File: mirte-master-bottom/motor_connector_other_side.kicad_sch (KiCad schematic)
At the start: 9 parts, among them J8 Motor_conn, U4 DRV8231DDAR

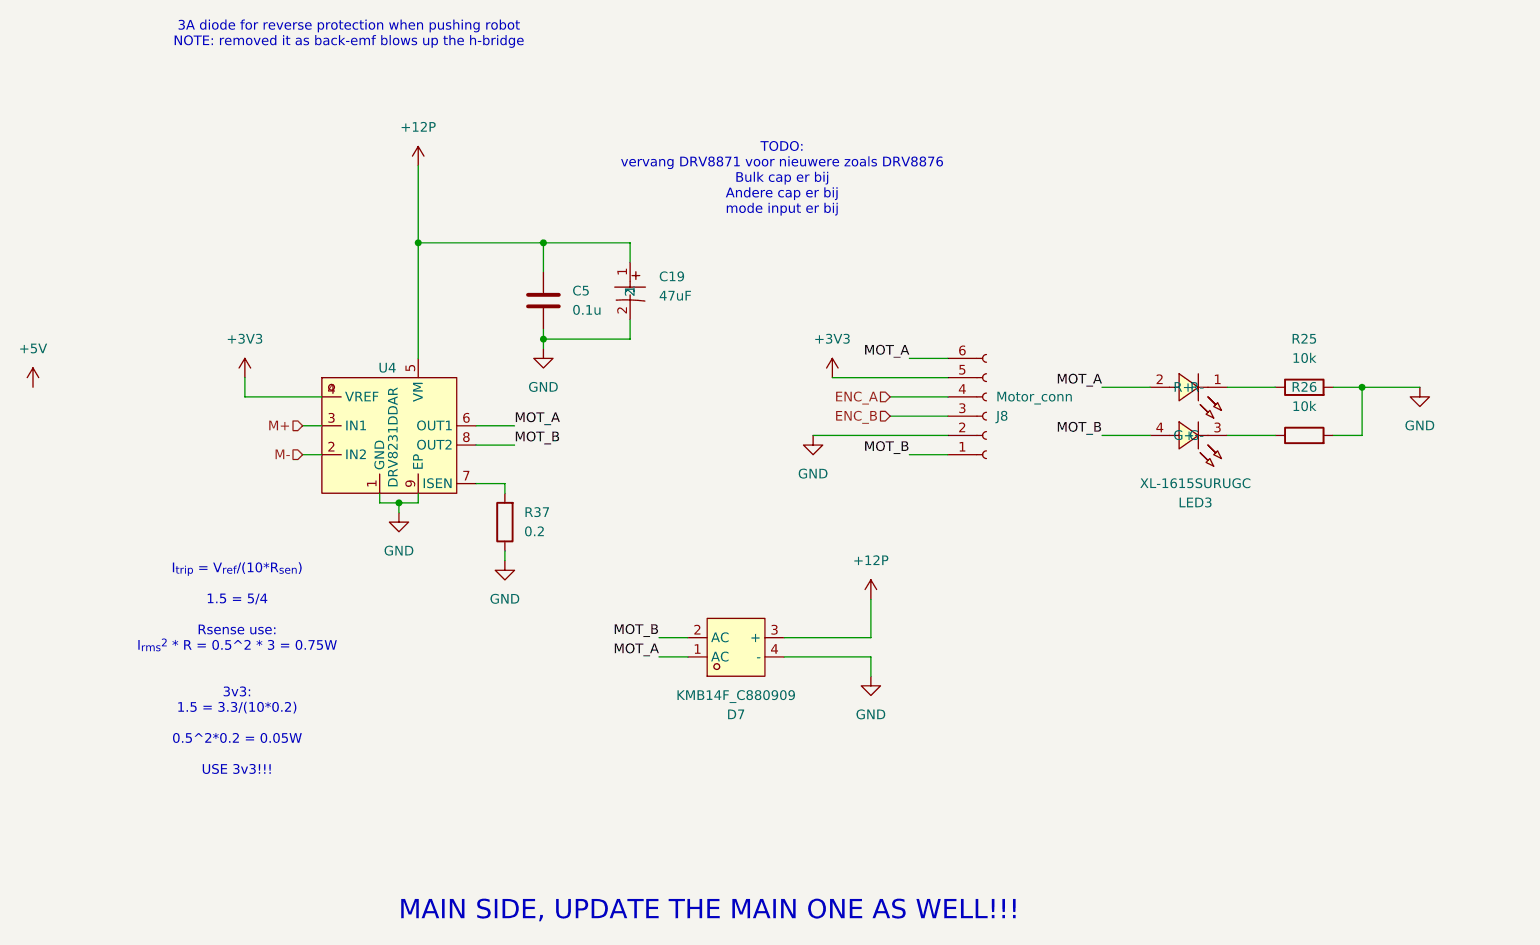
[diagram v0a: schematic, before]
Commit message: MM: motor leds same color, emergency button screw, start button led screw, drc exclusions
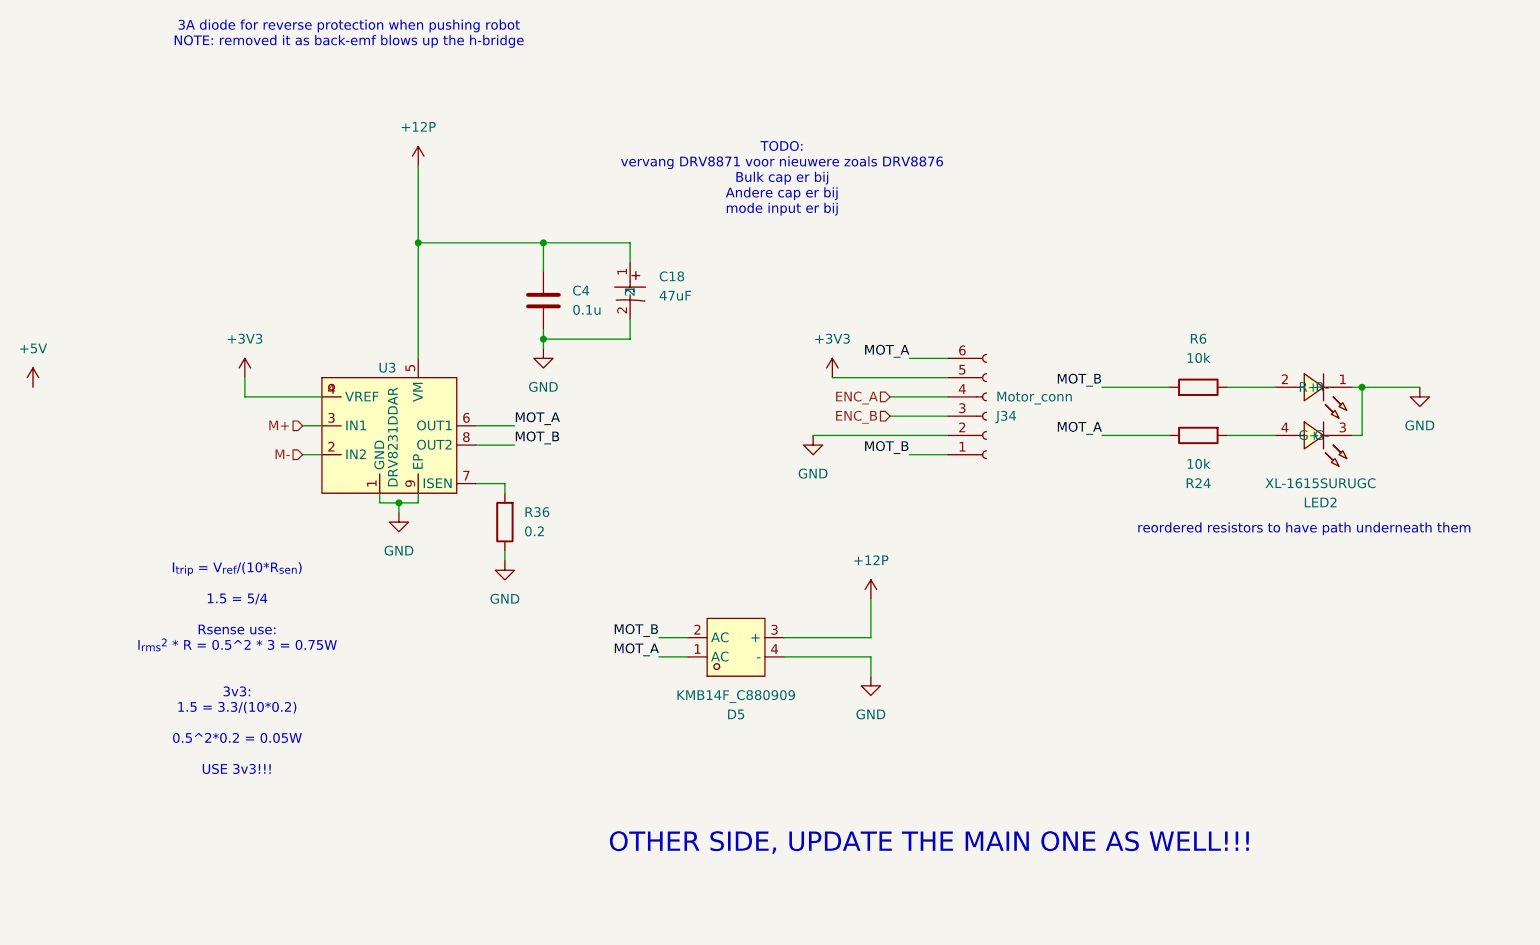
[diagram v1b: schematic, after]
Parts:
- renumbered C19 to C18, C5 to C4, D7 to D5, J8 to J34, LED3 to LED2, R26 to R24, R37 to R36, R25 to R6, U4 to U3
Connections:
- net GND: now also LED2.1 (R-), LED2.3 (G-); no longer R24.2, R6.2
- net MOT_A: now also R24.1; no longer LED2.2 (R+)
- net MOT_B: now also R6.2; no longer LED2.4 (G+)
- net at R6.1: now also LED2.2 (R+); no longer LED2.1 (R-)
- new net: LED2.4 (G+), R24.2
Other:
- note added: "OTHER SIDE, UPDATE THE MAIN ONE AS WELL!!!"
- note added: "reordered resistors to have path underneath them"
- note removed: "MAIN SIDE, UPDATE THE MAIN ONE AS WELL!!!"
- moved on the sheet: LED2, R24, R6

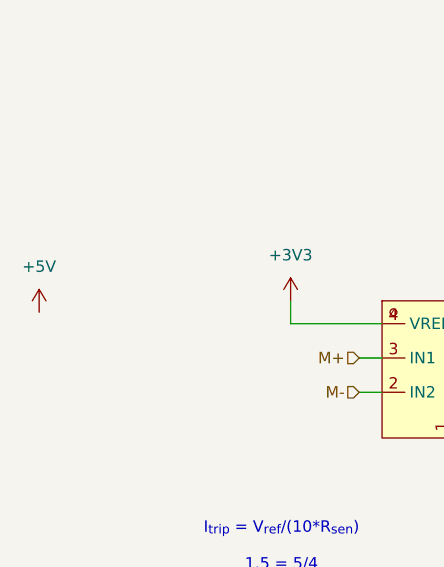
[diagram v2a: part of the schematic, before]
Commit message: MM: ERC&DRC fixes + change hbridge cap
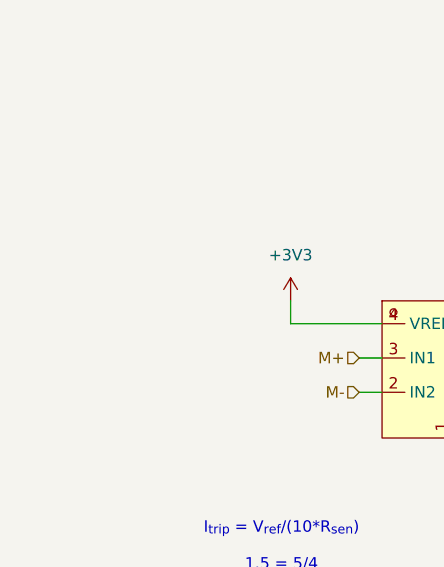
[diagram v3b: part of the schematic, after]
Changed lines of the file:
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@@
-	)
-	(symbol
-		(lib_id "power:+5V")
-		(at 11.43 72.39 0)
-		(unit 1)
-		(exclude_from_sim no)
-		(in_bom yes)
-		(on_board yes)
-		(dnp no)
-		(fields_autoplaced yes)
-		(property "Reference" "#PWR110"
-			(at 11.43 76.2 0)
-			(effects
-				(font
-					(size 1.27 1.27)
-				)
-				(hide yes)
-			)
-		)
-		(property "Value" "+5V"
-			(at 11.43 67.31 0)
-			(effects
-				(font
-					(size 1.27 1.27)
-				)
-			)
-		)
-		(property "Footprint" ""
-			(at 11.43 72.39 0)
-			(effects
-				(font
-					(size 1.27 1.27)
-				)
-				(hide yes)
-			)
-		)
-		(property "Datasheet" ""
-			(at 11.43 72.39 0)
-			(effects
-				(font
-					(size 1.27 1.27)
-				)
-				(hide yes)
-			)
-		)
-		(property "Description" "Power symbol creates a global label with name \"+5V\""
-			(at 11.43 72.39 0)
-			(effects
-				(font
-					(size 1.27 1.27)
-				)
-				(hide yes)
-			)
-		)
-		(pin "1"
-		)
-		(instances
-			(project "mirte-master-bottom"
-				(path "/c479422a-501d-4123-8665-56a1c70bd9ea/15e76074-7fdd-433c-b518-bfaad427cf18/66b45c4b-8e15-4752-bd0a-963e95885d51"
-					(reference "#PWR113")
-					(unit 1)
-				)
-				(path "/c479422a-501d-4123-8665-56a1c70bd9ea/15e76074-7fdd-433c-b518-bfaad427cf18/dae2003b-f49b-4b92-8a77-b6951156073a"
-					(reference "#PWR110")
-					(unit 1)
-				)
-			)
-		)
 	)
 	(symbol

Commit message: MM: order big
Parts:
- C18: LCSC (none) -> C3349
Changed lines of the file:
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@@
+			)
+		)
+		(property "LCSC" "C3349"
+			(at 93.98 57.8149 0)
+			(effects
+				(font
+					(size 1.27 1.27)
+				)
+				(hide yes)
 			)
 		)
